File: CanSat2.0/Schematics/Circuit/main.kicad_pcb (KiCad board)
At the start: 2 copper layers, 67.1 x 67.1 mm, 36 parts, among them J1 Center connector, J2 Middle connector, P1 CONN_2, P15 CONN_2, P2 CONN_2, P3 CONN_2, P4 CONN_2, SW7 SW_DIP_x01, U2 O2, U4 mg812_gas_sensor, U5 AD8572, U6 SP3_gas_sensor, U7 LMC662

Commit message: PCBs
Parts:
- added U1: LD1117S33TR_SOT223, TO_SOT_Packages_SMD:SOT-223-3_TabPin2, F.Cu at (40.2, 25.0)
- added U3: LD1117S50TR_SOT223, TO_SOT_Packages_SMD:SOT-223-3_TabPin2, F.Cu at (31.5, 32.6)
- C7, C8, J1, R1, R2, R3, R4, R5, R8, TH1, U5: moved to B.Cu
- moved U5 99.1 mm to (63.2, 65.0), turned to 270 degrees
- moved R2 98.5 mm to (64.3, 74.6), turned to 270 degrees
- moved R4 97.4 mm to (61.8, 75.3), turned to 180 degrees
- moved C7 97.2 mm to (61.8, 71.6)
- moved TH1 96.3 mm to (61.8, 73.9)
- moved R1 88.3 mm to (57.5, 67.0)
- moved R3 86.7 mm to (63.2, 59.3), turned to 180 degrees
- moved C8 85.6 mm to (56.0, 64.7), turned to 270 degrees
- moved R5 85.4 mm to (59.6, 61.2), turned to 180 degrees
- moved P4 78.6 mm to (60.7, 50.0), turned to 180 degrees
- moved R8 76.3 mm to (33.7, 68.5)
- moved U7 75.3 mm to (60.8, 25.6)
- moved R6 69.1 mm to (61.0, 32.4), turned to 90 degrees
- moved R34 66.8 mm to (58.4, 32.4)
- moved C2 66.3 mm to (42.1, 29.8), turned to 180 degrees
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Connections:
- J1 pad 13: (no net) -> Net-(J1-Pad13)
- J2 pad 16: (no net) -> Net-(J2-Pad16)
- U5 pad 5: (no net) -> Net-(U5-Pad5)
- U5 pad 6: (no net) -> Net-(U5-Pad6)
- U5 pad 7: (no net) -> Net-(U5-Pad7)
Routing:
- net GND: track 0.00 -> 293.9 mm, vias 0 -> 8
- net +5V: track 0.00 -> 161.0 mm, vias 0 -> 7
- net +BATT: track 0.00 -> 99.1 mm, vias 0 -> 1
- net +3V3: track 0.00 -> 97.0 mm, vias 0 -> 6
- net /CO2: track 0.00 -> 92.0 mm, vias 0 -> 2
- net /FC_PWM_6: track 0.00 -> 71.8 mm, vias 0 -> 2
- net /V_READ: track 0.00 -> 66.5 mm, vias 0 -> 5
- net /RFM_SS: track 0.00 -> 63.5 mm, vias 0 -> 6
- net Net-(P1-Pad2): track 0.00 -> 61.2 mm, vias 0 -> 3
- net Net-(P2-Pad2): track 0.00 -> 61.1 mm, vias 0 -> 2
- net /FC_PWM_4: track 0.00 -> 59.8 mm, vias 0 -> 2
- net /FC_PWM_8: track 0.00 -> 49.7 mm, vias 0 -> 7
- net /SDA: track 0.00 -> 43.9 mm, vias 0 -> 3
- net /SERVO: track 0.00 -> 40.2 mm, vias 0 -> 1
- net /MISO: track 0.00 -> 36.8 mm
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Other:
- board size 67.1 x 67.1 mm -> 64 x 64 mm

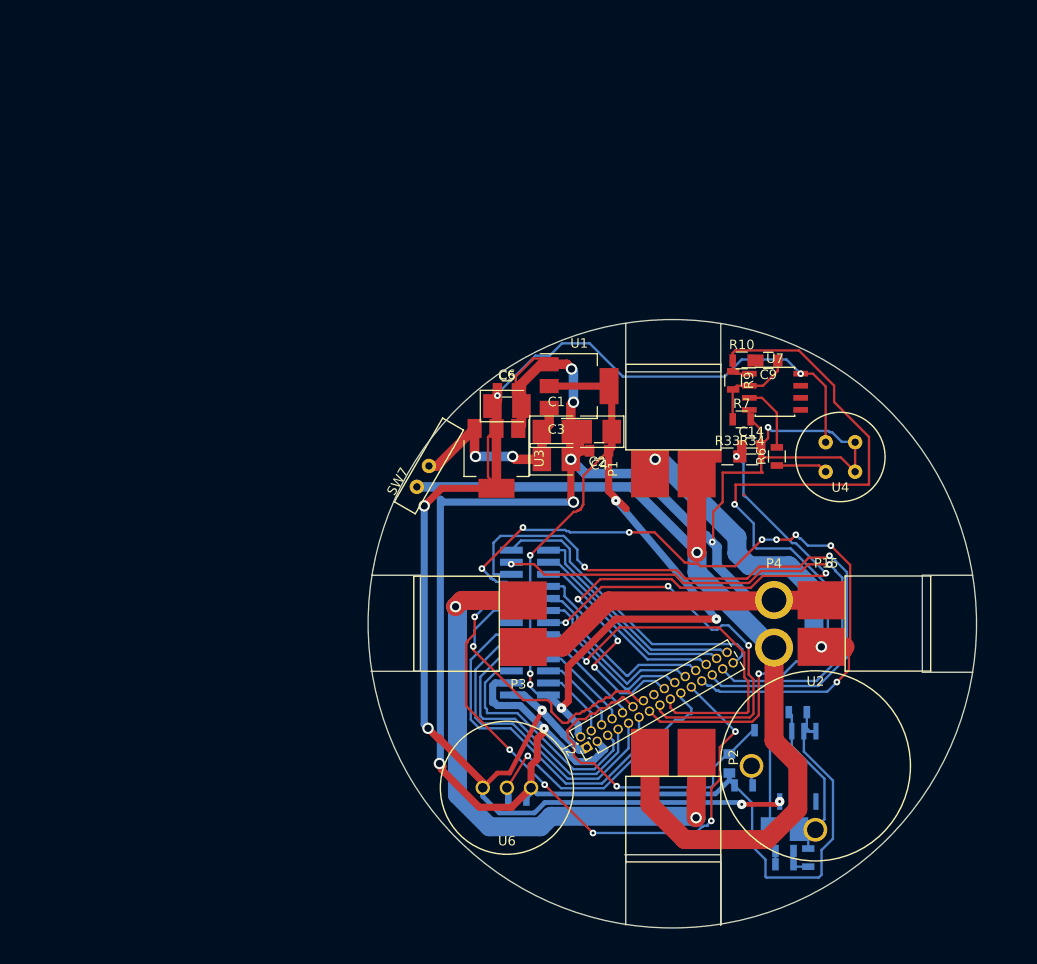
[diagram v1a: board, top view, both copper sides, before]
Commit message: Add three top boards and some other circuitry and modelling
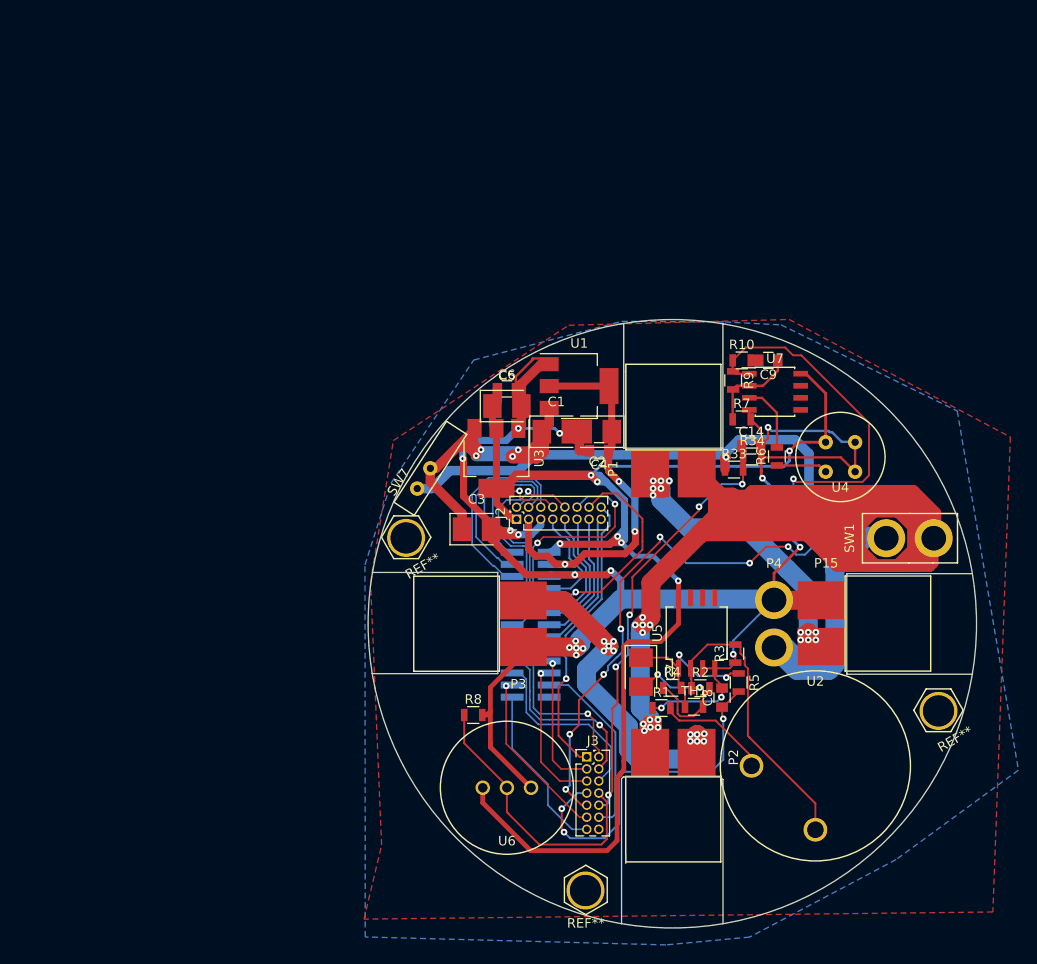
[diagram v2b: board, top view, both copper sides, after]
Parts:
- added J3: Conn_02x07_Counter_Clockwise, Pin_Headers:Pin_Header_Straight_2x07_Pitch1.27mm, F.Cu at (41.0, 64.0)
- added REF**: Standoff, CanSat:Standoff, F.Cu at (78.0, 59.1)
- added REF**: Standoff, CanSat:Standoff, F.Cu at (40.9, 78.0)
- added REF**: Standoff, CanSat:Standoff, F.Cu at (22.0, 40.9)
- added SW1: SW_DIP_x01, CanSat:TX30_vertical, F.Cu at (75.0, 41.0)
- C7, C8, R1, R2, R3, R4, R5, R8, TH1, U5: moved to F.Cu
- J2: value Middle connector -> Conn_02x08_Counter_Clockwise; footprint Pin_Headers:Pin_Header_Straight_2x15_Pitch1.27mm -> Pin_Headers:Pin_Header_Straight_2x08_Pitch1.27mm
- moved J2 25.1 mm to (33.6, 39.0), turned to 90 degrees
- moved C7 22.4 mm to (46.7, 55.1), turned to 270 degrees
- moved R4 22.0 mm to (50.0, 56.7), turned to 0 degrees
- moved R2 21.1 mm to (53.0, 56.8), turned to 0 degrees
- moved TH1 17.9 mm to (52.3, 58.7)
- moved U5 17.6 mm to (52.6, 51.0), turned to 90 degrees
- moved R1 11.9 mm to (48.9, 58.9)
- moved C3 11.2 mm to (29.4, 40.0)
- moved R8 10.0 mm to (29.1, 59.6)
- moved R3 9.01 mm to (56.6, 53.1), turned to 90 degrees
- moved C8 6.97 mm to (55.2, 57.8), turned to 90 degrees
- moved R5 5.66 mm to (57.0, 56.2), turned to 270 degrees
- moved R33 1.54 mm to (56.5, 33.8)
- moved SW7 0.29 mm to (24.6, 33.6), turned to 237 degrees
- moved J1 0.24 mm to (35.1, 50.1), turned to 180 degrees
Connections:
- J1 pad 10: /SCK -> /FC_PWM_5
- J1 pad 11: /MISO -> /GSM_SLP
- J1 pad 12: /SERVO -> /FC_PWM_6
- J1 pad 13: Net-(J1-Pad13) -> /GSM_KEY
- J1 pad 14: /SDA -> /FC_PWM_7
- J1 pad 15: /SCL -> /GSM_TX
- J1 pad 16: /MOSI -> /FC_PWM_8
- J1 pad 17: /RFM_SS -> /GSM_RX
- J1 pad 19: /FC_PWM_8 -> /SCK
- J1 pad 2: +3V3 -> /FC_PWM_1
- J1 pad 20: /FC_PWM_7 -> /RFM_SS
- J1 pad 21: /FC_PWM_6 -> /MISO
- J1 pad 22: /FC_PWM_5 -> /MOSI
- J1 pad 23: /FC_PWM_4 -> /SERVO
- J1 pad 24: /FC_PWM_3 -> /SCL
- J1 pad 25: /FC_PWM_2 -> (no net)
- J1 pad 26: /FC_PWM_1 -> /SDA
- J1 pad 3: GND -> +3V3
- J1 pad 4: /CAM_EN -> /FC_PWM_2
- J1 pad 5: /FC_EN -> GND
- J1 pad 6: /GSM_SLP -> /FC_PWM_3
- J1 pad 7: /GSM_KEY -> /CAM_EN
- J1 pad 8: /GSM_TX -> /FC_PWM_4
- J1 pad 9: /GSM_RX -> /FC_EN
- J2 pad 10: /SCK -> /FC_PWM_5
- J2 pad 11: /MISO -> /GSM_SLP
- J2 pad 12: /O2 -> /FC_PWM_6
- J2 pad 13: /CO2 -> /GSM_KEY
- J2 pad 14: /SCL -> /FC_PWM_7
- J2 pad 15: /SDA -> /GSM_TX
- J2 pad 16: Net-(J2-Pad16) -> /FC_PWM_8
- J2 pad 2: +3V3 -> /FC_PWM_1
- J2 pad 3: GND -> +3V3
- J2 pad 4: /CAM_EN -> /FC_PWM_2
- J2 pad 5: /FC_EN -> GND
- J2 pad 6: /GSM_SLP -> /FC_PWM_3
- J2 pad 7: /GSM_KEY -> /CAM_EN
- J2 pad 8: /GSM_TX -> /FC_PWM_4
- J2 pad 9: /GSM_RX -> /FC_EN
- P1 pad 1: +BATT -> Net-(P1-Pad1)
- P2 pad 1: +BATT -> Net-(P1-Pad1)
- U5 pad 5: Net-(U5-Pad5) -> (no net)
- U5 pad 6: Net-(U5-Pad6) -> (no net)
- U5 pad 7: Net-(U5-Pad7) -> (no net)
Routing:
- net Net-(P1-Pad1): track 0.00 -> 246.4 mm, vias 0 -> 11
- net GND: track 293.9 -> 205.5 mm, vias 8 -> 18
- net +3V3: track 97.0 -> 44.0 mm, vias 6 -> 3
- net /FC_PWM_6: track 71.8 -> 25.0 mm
- net /RFM_SS: track 63.5 -> 19.7 mm, vias 6 -> 1
- net /FC_PWM_4: track 59.8 -> 21.7 mm, vias 2 -> 1
- net /FC_PWM_8: track 49.7 -> 22.3 mm, vias 7 -> 0
- net /SDA: track 43.9 -> 18.1 mm, vias 3 -> 0
- net Net-(C7-Pad2): track 18.2 -> 41.2 mm, vias 0 -> 2
- net /MISO: track 36.8 -> 15.9 mm, vias 0 -> 1
- net /SERVO: track 40.2 -> 19.5 mm, vias 1 -> 0
- net Net-(C1-Pad1): track 22.2 -> 42.9 mm, vias 2 -> 4
- net /V_READ: track 66.5 -> 47.0 mm
- net +5V: track 161.0 -> 141.7 mm
- net /GSM_RX: track 32.6 -> 15.6 mm, vias 0 -> 1
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- added copper zone on B.Cu, net +BATT
- added copper zone on F.Cu, net GND
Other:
- outline, holes or cut-outs redrawn
- net class Default: clearance 0.203 -> 0.17; trace_width 0.25 -> 0.17
- rule trace_clearance: 0.203 -> 0.17
- rule trace_min: 0.203 -> 0.165

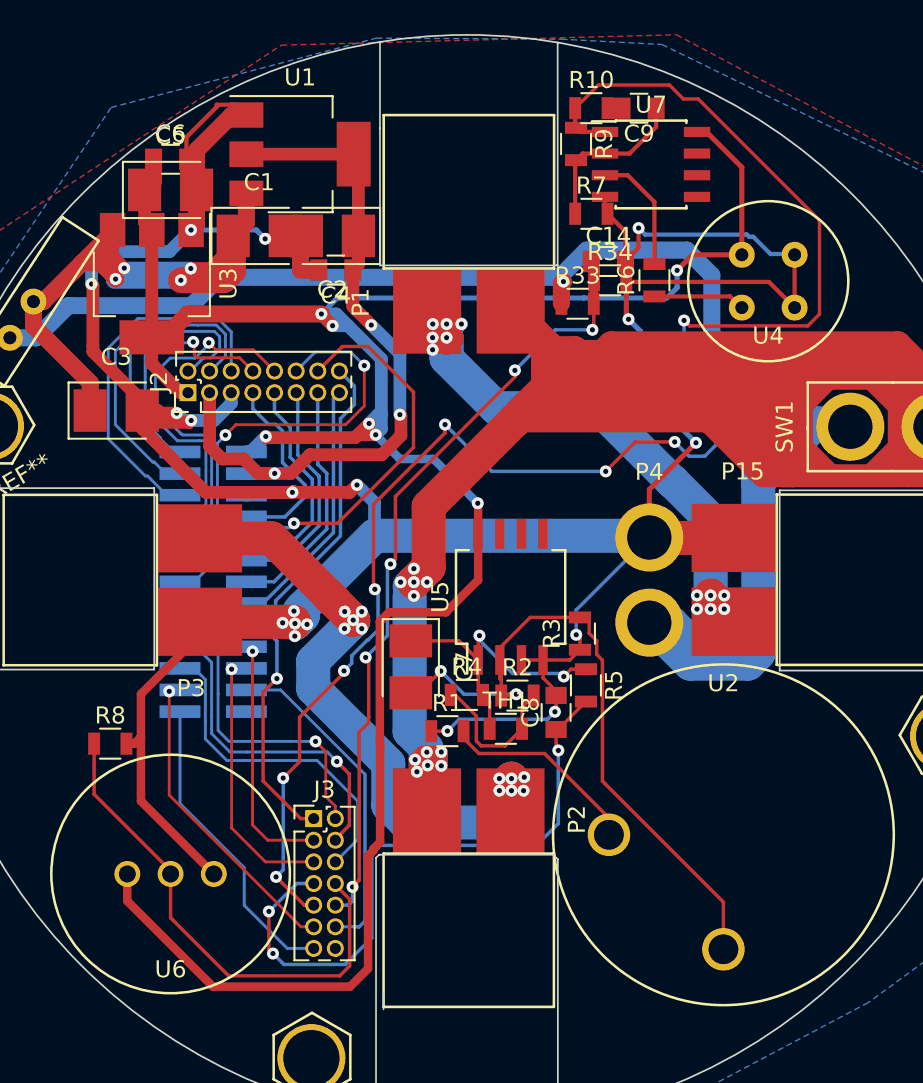
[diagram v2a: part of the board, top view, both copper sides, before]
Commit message: Add new pcbs - center and bottom - and fill the lower half of the model
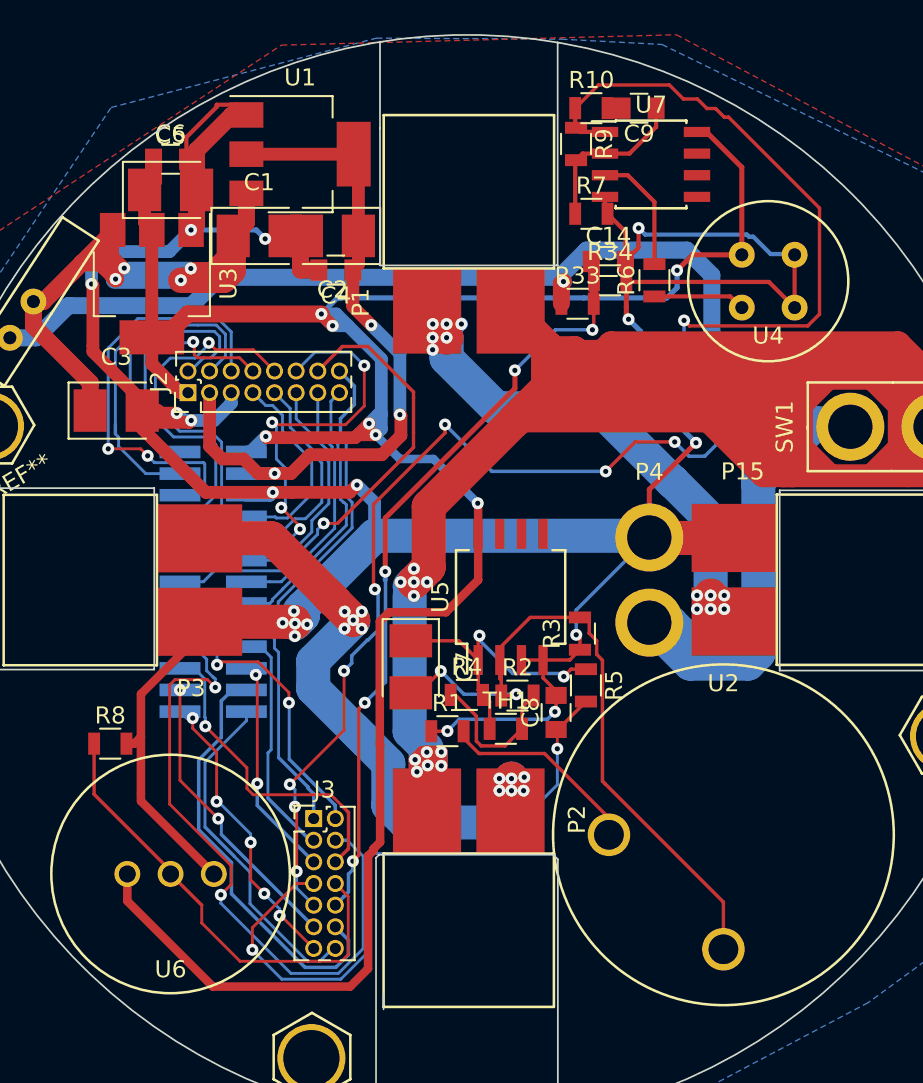
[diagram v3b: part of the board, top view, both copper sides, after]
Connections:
- net /MISO renamed /MISOLOW
- net /MOSI renamed /MOSILOW
- net /SCK renamed /SCKLOW
- J1 pad 25: (no net) -> /GAMMA
- J3 pad 14: (no net) -> /GAMMA
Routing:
- net /GAMMA: track 0.00 -> 20.1 mm
- net /RFM_SS: track 19.7 -> 39.4 mm, vias 1 -> 2
- net /SERVO: track 19.5 -> 26.2 mm
- net /FC_PWM_6: track 25.0 -> 28.0 mm, vias 2 -> 4
- net /MISOLOW: track 15.9 -> 13.1 mm, vias 1 -> 2
- net /FC_PWM_3: track 23.1 -> 25.4 mm, vias 0 -> 2
- net /GSM_RX: track 15.6 -> 13.5 mm, vias 1 -> 0
- net /O3: track 29.6 -> 27.4 mm
- net /GSM_TX: track 15.2 -> 16.7 mm
- net /RFM_INT: track 18.7 -> 17.3 mm, vias 1 -> 2
- net /SCL: track 18.4 -> 17.2 mm, vias 1 -> 2
- net GND: track 205.5 -> 204.3 mm
- net /SCKLOW: track 15.0 -> 13.8 mm, vias 1 -> 0
- net /O2: track 37.3 -> 38.4 mm, vias 3 -> 2
- net /MOSILOW: track 19.8 -> 19.0 mm, vias 0 -> 1
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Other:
- net class Default: clearance 0.17 -> 0.165
- rule trace_clearance: 0.17 -> 0.165

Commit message: Edit final version of pcbs, gerbers generated
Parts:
- added C10: 100 nF, Capacitors_SMD:C_0805, F.Cu at (65.2, 25.8)
- added C11: 100 nF, Capacitors_SMD:C_0805, F.Cu at (53.4, 45.2)
- U6: moved to B.Cu
- moved R8 7.15 mm to (22.0, 58.4), turned to 90 degrees
- moved U6 1.05 mm to (31.7, 67.8)
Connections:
- J3 pad 11: /SCL -> /O3
- J3 pad 12: /SERVO -> /MOSILOW
- J3 pad 13: /SDA -> /RFM_SS
- J3 pad 14: /GAMMA -> /RFM_INT
- J3 pad 2: /RFM_INT -> /SCKLOW
- J3 pad 3: /SCKLOW -> /MISOLOW
- J3 pad 4: /RFM_SS -> /O2
- J3 pad 5: /MISOLOW -> /CO2
- J3 pad 6: /MOSILOW -> /SCL
- J3 pad 7: /O2 -> /SDA
- J3 pad 8: /O3 -> /GAMMA
- J3 pad 9: /CO2 -> /SERVO
- U5 pad 5: (no net) -> GND
- U5 pad 6: (no net) -> GND
- U7 pad 5: (no net) -> GND
- U7 pad 6: (no net) -> GND
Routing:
- net GND: track 204.3 -> 224.6 mm, vias 18 -> 21
- net /O2: track 38.4 -> 26.9 mm, vias 2 -> 3
- net /SCL: track 17.2 -> 27.5 mm, vias 2 -> 3
- net /MOSILOW: track 19.0 -> 28.9 mm, vias 1 -> 3
- net /SERVO: track 26.2 -> 16.8 mm
- net /RFM_INT: track 17.3 -> 26.6 mm
- net Net-(P1-Pad1): track 246.4 -> 239.3 mm
- net /RFM_SS: track 39.4 -> 32.5 mm, vias 2 -> 3
- net /GAMMA: track 20.1 -> 14.4 mm, vias 0 -> 1
- net +5V: track 141.2 -> 146.6 mm
- net /O3: track 27.4 -> 31.0 mm, vias 0 -> 1
- net /SDA: track 17.5 -> 14.0 mm, vias 5 -> 1
- net /CO2: track 95.0 -> 92.2 mm
- net +BATT: track 91.6 -> 89.3 mm
- net /SCKLOW: track 13.8 -> 15.8 mm, vias 0 -> 1
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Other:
- outline, holes or cut-outs redrawn
- net class Default: clearance 0.165 -> 0.163
- rule trace_clearance: 0.165 -> 0.163
